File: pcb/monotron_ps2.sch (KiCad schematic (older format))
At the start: 7 parts, among them J13 DB25_Female, J14 Mini-DIN-6, J15 Mini-DIN-6, U5 ATmega48A-PU

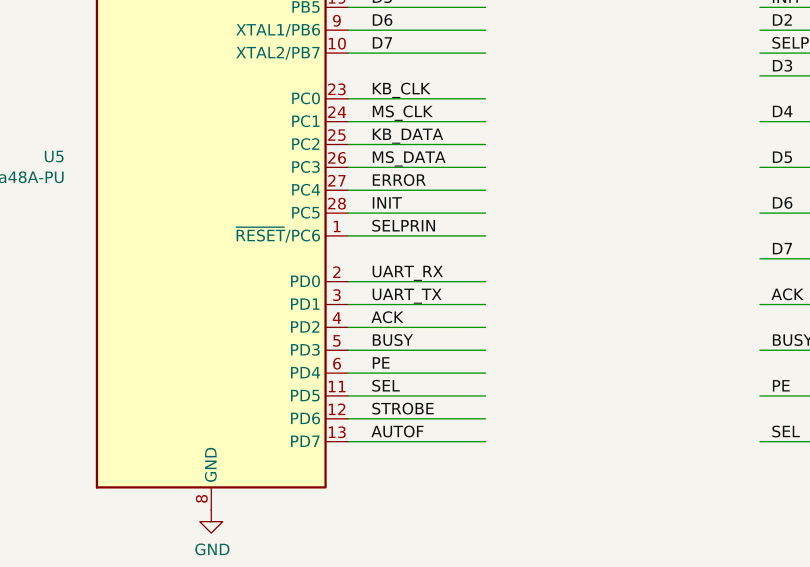
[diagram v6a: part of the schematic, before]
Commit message: Moved some pins around to ease the routing.
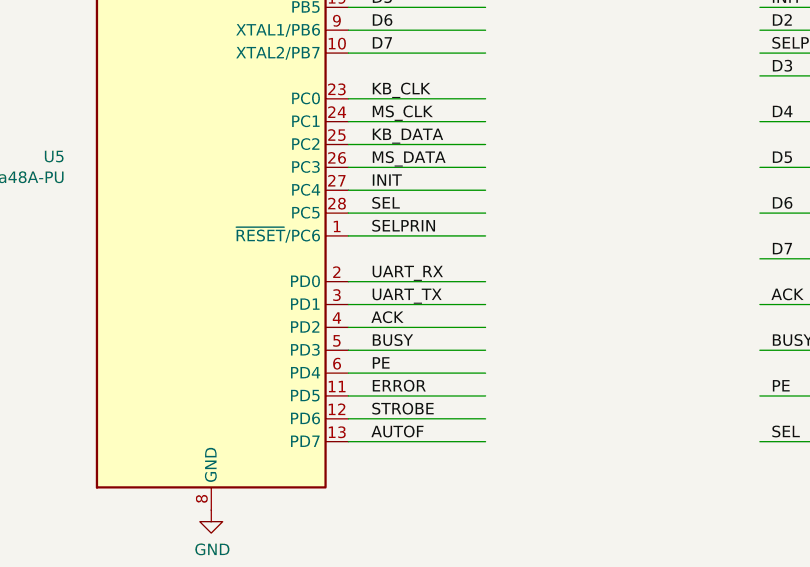
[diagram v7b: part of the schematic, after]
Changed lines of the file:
@@
 PE
 Text Label 4600 4050 0    50   ~ 0
-SEL
+ERROR
 Text Label 4600 4150 0    50   ~ 0
 STROBE
@@
 AUTOF
 Text Label 4600 3150 0    50   ~ 0
-ERROR
+INIT
 Text Label 4600 3250 0    50   ~ 0
-INIT
+SEL
 Wire Wire Line
 	4500 3350 5100 3350

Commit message: Adjusted component layout again. ) More room between MIDI connectors. ) SD/MMC connector now under Launchpad board
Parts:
- J14, J15: footprint Launchpad:mini-DIN 6 -> Monotron:mini-DIN 6
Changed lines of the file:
@@
 F 0 "J14" H 9000 3117 50  0000 C CNN
 F 1 "Mini-DIN-6" H 9000 3026 50  0000 C CNN
-F 2 "Launchpad:mini-DIN 6" H 9000 2750 50  0001 C CNN
+F 2 "Monotron:mini-DIN 6" H 9000 2750 50  0001 C CNN
 F 3 "https://www.te.com/commerce/DocumentDelivery/DDEController?Action=srchrtrv&DocNm=5749180&DocType=Customer+Drawing&DocLang=English" H 9000 2750 50  0001 C CNN
 F 4 "5749180-1-ND" H 9000 2750 50  0001 C CNN "Digikey"
@@
 F 0 "J15" H 9000 4267 50  0000 C CNN
 F 1 "Mini-DIN-6" H 9000 4176 50  0000 C CNN
-F 2 "Launchpad:mini-DIN 6" H 9000 3900 50  0001 C CNN
+F 2 "Monotron:mini-DIN 6" H 9000 3900 50  0001 C CNN
 F 3 "https://www.te.com/commerce/DocumentDelivery/DDEController?Action=srchrtrv&DocNm=5749180&DocType=Customer+Drawing&DocLang=English" H 9000 3900 50  0001 C CNN
 F 4 "5749180-1-ND" H 9000 3900 50  0001 C CNN "Digikey"
